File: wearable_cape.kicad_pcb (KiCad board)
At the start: 2 copper layers, 48 parts, among them P1 BELA_AINS, P2 RECEIVER, P3 BATTERY, P4 BELA_AOUTS, P5 CONN_01X04, P6 CONN_01X04, P7 CONN_01X04, SW1 SW_HALT, SW2 SW_MODE_SEL, U1 MCP6004, U2 MCP6004, U3 BEAGLEBONEBLACK, U4 OKI_7805

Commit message: basic routing done
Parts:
- added C20: 100nF, Capacitors_SMD:C_0603_HandSoldering, F.Cu at (87.6, 49.5)
- moved R1 34.7 mm to (88.3, 27.3)
- moved SW1 32.7 mm to (88.9, 31.8)
- moved R9 7.62 mm to (67.3, 58.4)
- moved R5 5.08 mm to (74.9, 58.4)
- moved R4 5.08 mm to (72.4, 58.4)
- moved R12 3.42 mm to (95.2, 68.6)
- moved R8 2.54 mm to (69.8, 58.4)
- moved SW2 1.27 mm to (102.2, 68.6)
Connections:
- C5 pad 2: GND -> GNDA
- P2 pad 2: /RCV0 -> /D15
- P2 pad 4: /RCV1 -> /D14
- P2 pad 6: /RCV2 -> /D13
- P2 pad 8: /RCV3 -> /D12
- P4 pad 10: Net-(P4-Pad10) -> GNDA
- P4 pad 9: Net-(P4-Pad9) -> VCC
- P5 pad 1: /FILT_OUT0 -> /FILT_OUT1
- P5 pad 2: /FILT_OUT1 -> /FILT_OUT0
- R2 pad 1: SYS_5V -> VCC
- R3 pad 2: GND -> GNDA
- R4 pad 2: /BELA_OUT0 -> /BELA_OUT2
- R5 pad 2: /BELA_OUT1 -> /BELA_OUT3
- R8 pad 2: /BELA_OUT2 -> /BELA_OUT1
- R9 pad 2: /BELA_OUT3 -> /BELA_OUT0
- U1 pad 11: GND -> GNDA
- U2 pad 11: GND -> GNDA
- U3 pad B10: /D2 -> /D3
- U3 pad B11: Net-(U3-PadB11) -> /D4
- U3 pad B12: /D4 -> /D5
- U3 pad B15: Net-(U3-PadB15) -> /D8
- U3 pad B16: /D8 -> /D9
- U3 pad B18: Net-(U3-PadB18) -> /D11
- U3 pad B2: Net-(U3-PadB2) -> GND
- U3 pad B27: /~HALT -> /D12
- U3 pad B28: /D12 -> /D13
- U3 pad B29: Net-(U3-PadB29) -> /D14
- U3 pad B3: SYS_3.3V -> Net-(U3-PadB3)
- U3 pad B30: /D14 -> /D15
- U3 pad B37: Net-(U3-PadB37) -> /TX
- U3 pad B38: Net-(U3-PadB38) -> /RX
- U3 pad B5: RAW_5V -> Net-(U3-PadB5)
- U3 pad B7: SYS_5V -> /D0
- U3 pad B8: /D0 -> /D1
- U3 pad B9: Net-(U3-PadB9) -> /D2
- U3 pad C10: /D3 -> Net-(U3-PadC10)
- U3 pad C11: /D6 -> Net-(U3-PadC11)
- U3 pad C12: /D5 -> /D6
- U3 pad C13: /D7 -> Net-(U3-PadC13)
- U3 pad C14: Net-(U3-PadC14) -> /D7
- U3 pad C15: /D10 -> Net-(U3-PadC15)
- U3 pad C16: /D9 -> /D10
- U3 pad C18: /D11 -> Net-(U3-PadC18)
- U3 pad C2: Net-(U3-PadC2) -> GND
- U3 pad C27: Net-(U3-PadC27) -> /~HALT
- U3 pad C28: /D13 -> Net-(U3-PadC28)
- U3 pad C30: /D15 -> Net-(U3-PadC30)
- U3 pad C4: Net-(U3-PadC4) -> SYS_3.3V
- U3 pad C43: Net-(U3-PadC43) -> GND
- U3 pad C44: Net-(U3-PadC44) -> GND
- U3 pad C45: Net-(U3-PadC45) -> GND
- U3 pad C46: Net-(U3-PadC46) -> GND
- U3 pad C6: Net-(U3-PadC6) -> RAW_5V
- U3 pad C7: Net-(U3-PadC7) -> SYS_5V
- U3 pad C8: /D1 -> Net-(U3-PadC8)
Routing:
- net GND: track 0.00 -> 135.3 mm, vias 0 -> 2
- net RAW_5V: track 0.00 -> 115.8 mm
- net BAT_11.1V: track 0.00 -> 110.1 mm
- net VCC: track 0.00 -> 63.7 mm, vias 0 -> 4
- net GNDA: track 0.00 -> 60.4 mm, vias 0 -> 2
- net /FILT_OUT5: track 0.00 -> 58.6 mm, vias 0 -> 2
- net SYS_3.3V: track 0.00 -> 54.1 mm
- net /FILT_OUT4: track 0.00 -> 53.1 mm, vias 0 -> 2
- net REF_1.8V: track 0.00 -> 52.9 mm, vias 0 -> 4
- net /FILT_OUT0: track 0.00 -> 45.2 mm, vias 0 -> 1
- net /FILT_OUT1: track 0.00 -> 43.2 mm, vias 0 -> 2
- net /~HALT: track 0.00 -> 34.3 mm
- net /FILT_OUT2: track 0.00 -> 32.1 mm
- net Net-(C10-Pad2): track 0.00 -> 31.4 mm, vias 0 -> 2
- net /D15: track 0.00 -> 31.4 mm
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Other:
- net class BAT added: clearance 0.3, trace_width 0.5, via_dia 1, via_drill 0.6

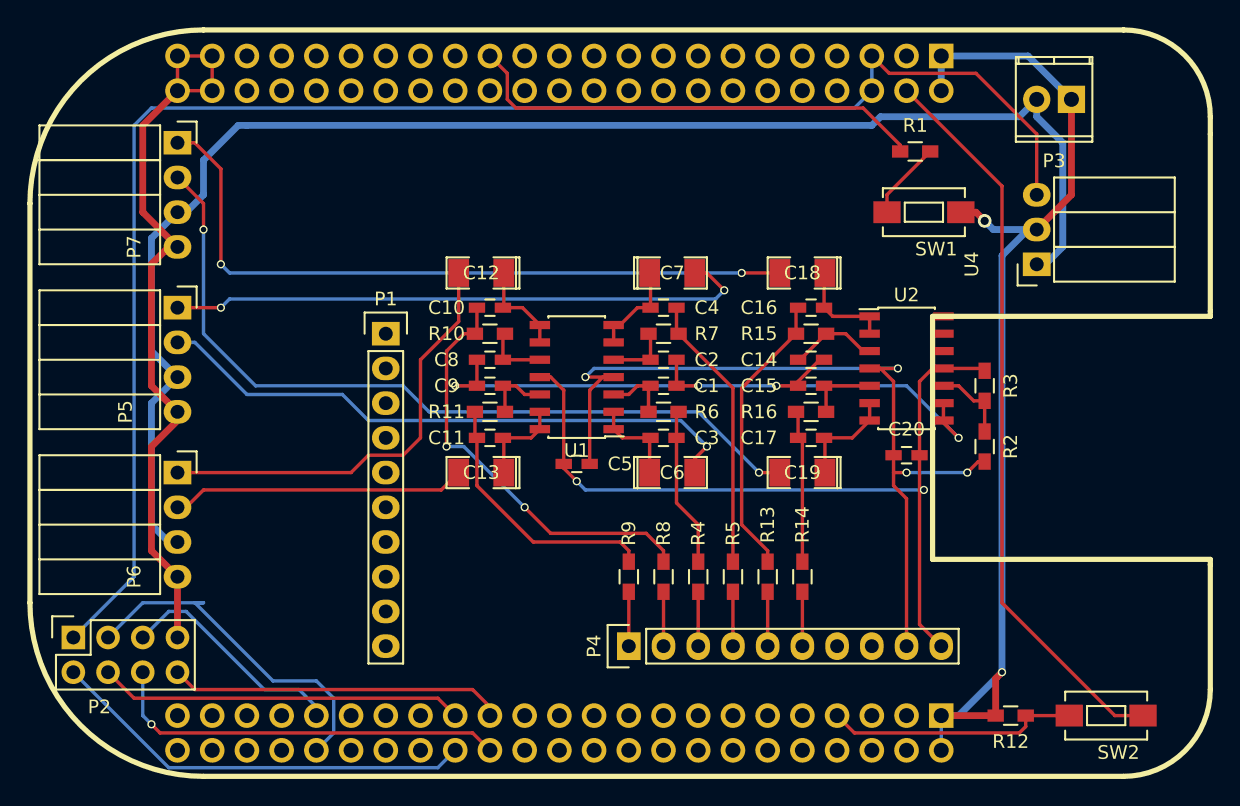
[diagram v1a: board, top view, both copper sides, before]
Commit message: added zones
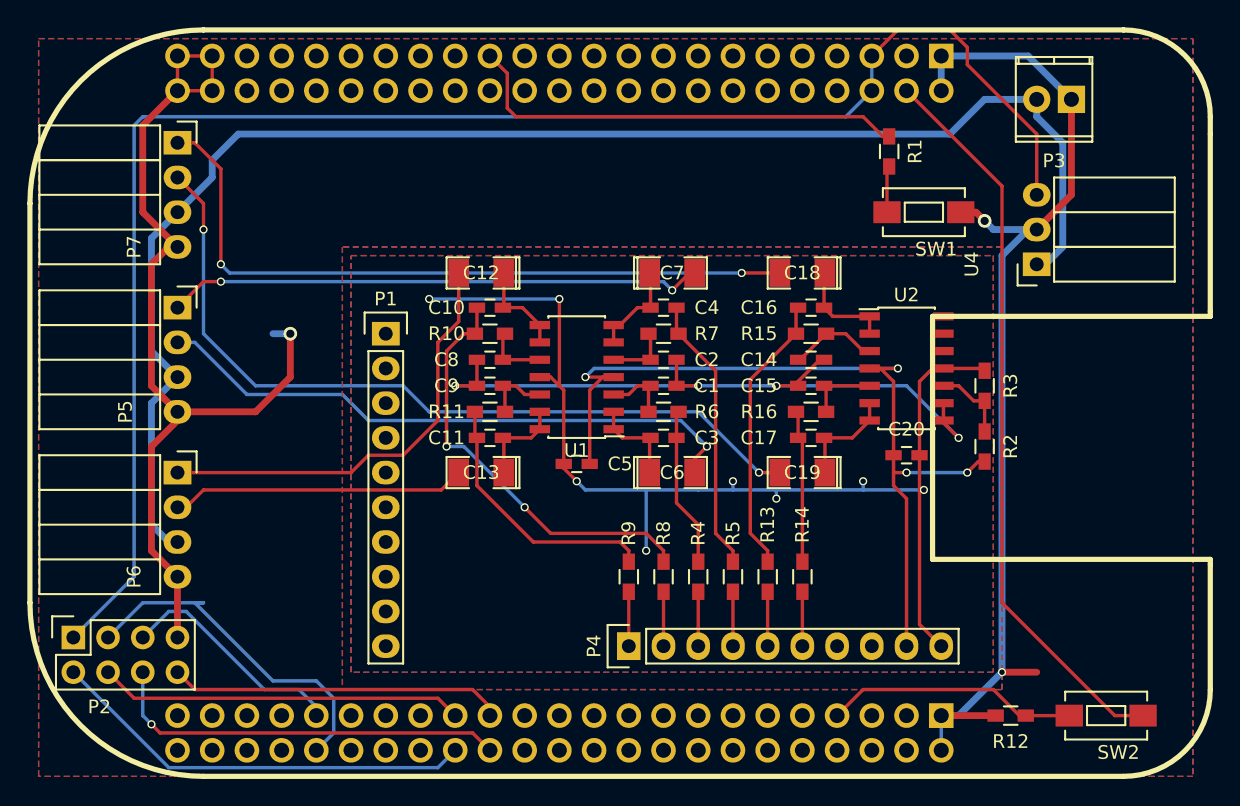
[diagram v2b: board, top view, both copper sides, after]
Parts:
- moved R1 1.91 mm to (86.4, 27.3), turned to 270 degrees
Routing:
- net GNDA: track 60.4 -> 82.7 mm, vias 2 -> 8
- net GND: track 135.3 -> 148.2 mm, vias 2 -> 3
- net /FILT_OUT1: track 43.2 -> 39.4 mm
- net Net-(R1-Pad2): track 5.76 -> 3.41 mm
- net RAW_5V: track 115.8 -> 118.1 mm
- net /~HALT: track 34.3 -> 33.1 mm
- net Net-(C16-Pad2): track 21.1 -> 20.6 mm
- added copper zone on B.Cu, net GND
- added copper zone on F.Cu, net GND
- added copper zone on B.Cu, net GNDA
- added copper zone on F.Cu, net GNDA

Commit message: Updates to PCB and first BOM files
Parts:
- added C21: CP1, SMD_Packages:SMD-1210_Pol, F.Cu at (91.2, 34.8)
- added C22: CP1, SMD_Packages:SMD-1210_Pol, F.Cu at (93.0, 29.2)
- moved SW2 7.75 mm to (97.8, 62.2), turned to 270 degrees
- moved P2 7.62 mm to (34.3, 62.9)
- moved P5 7.62 mm to (41.9, 38.7)
- moved P6 7.62 mm to (41.9, 50.8)
- moved P7 7.62 mm to (41.9, 26.7)
- moved R1 5.64 mm to (80.9, 28.7)
- moved SW1 3.78 mm to (86.4, 29.0)
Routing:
- net GND: track 148.2 -> 195.3 mm, vias 3 -> 1
- net SYS_3.3V: track 54.1 -> 42.4 mm
- net /FILT_OUT4: track 53.1 -> 41.5 mm, vias 2 -> 0
- net /FILT_OUT0: track 45.2 -> 35.6 mm
- net /FILT_OUT2: track 32.1 -> 23.1 mm
- net /FILT_OUT3: track 21.6 -> 14.0 mm
- net /D14: track 26.7 -> 19.1 mm
- net /D13: track 29.6 -> 22.0 mm, vias 1 -> 0
- net /D12: track 24.5 -> 17.7 mm
- net /D15: track 31.4 -> 24.5 mm
- net /FILT_OUT1: track 39.4 -> 33.8 mm, vias 2 -> 0
- net /RX: track 26.1 -> 20.5 mm
- net BAT_11.1V: track 110.0 -> 105.5 mm
- net /FILT_OUT5: track 58.6 -> 54.2 mm
- net /~HALT: track 33.1 -> 28.8 mm
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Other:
- board outline added: 70.5 x 54.6 mm

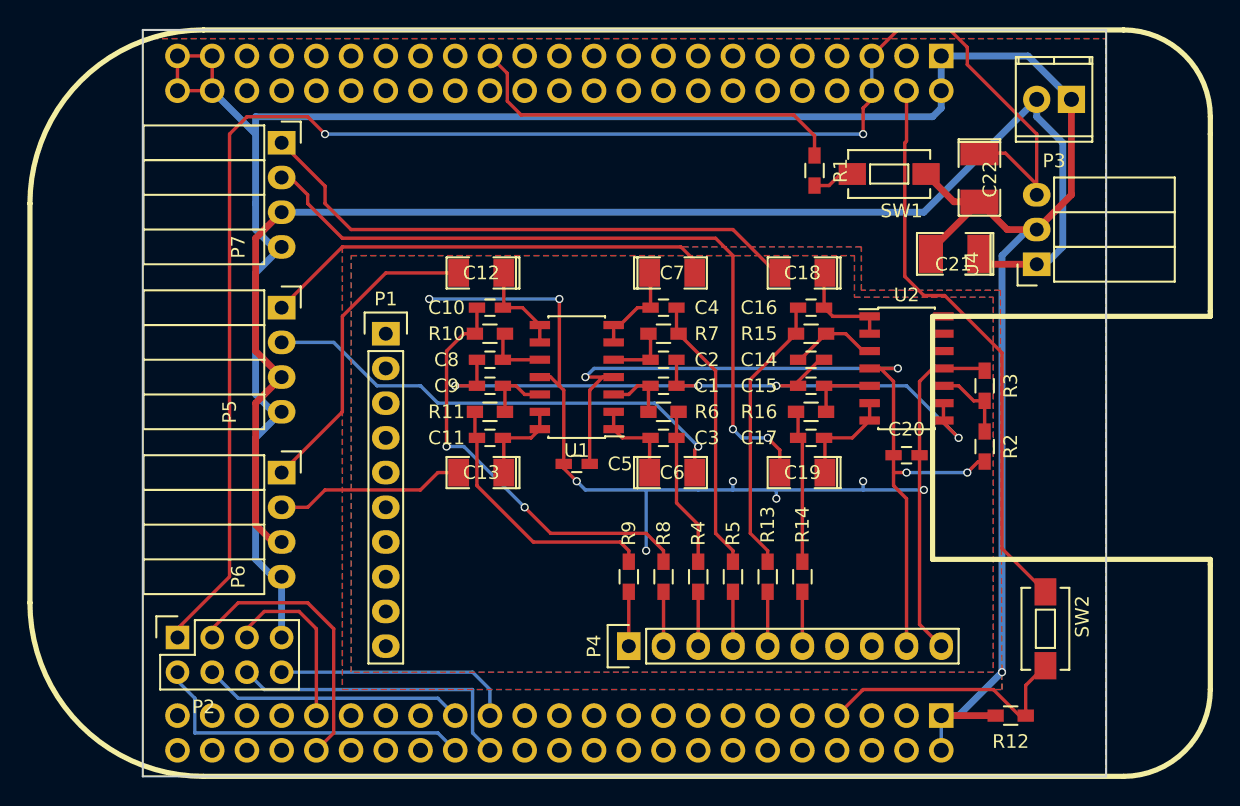
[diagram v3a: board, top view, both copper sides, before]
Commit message: Fill in zones better
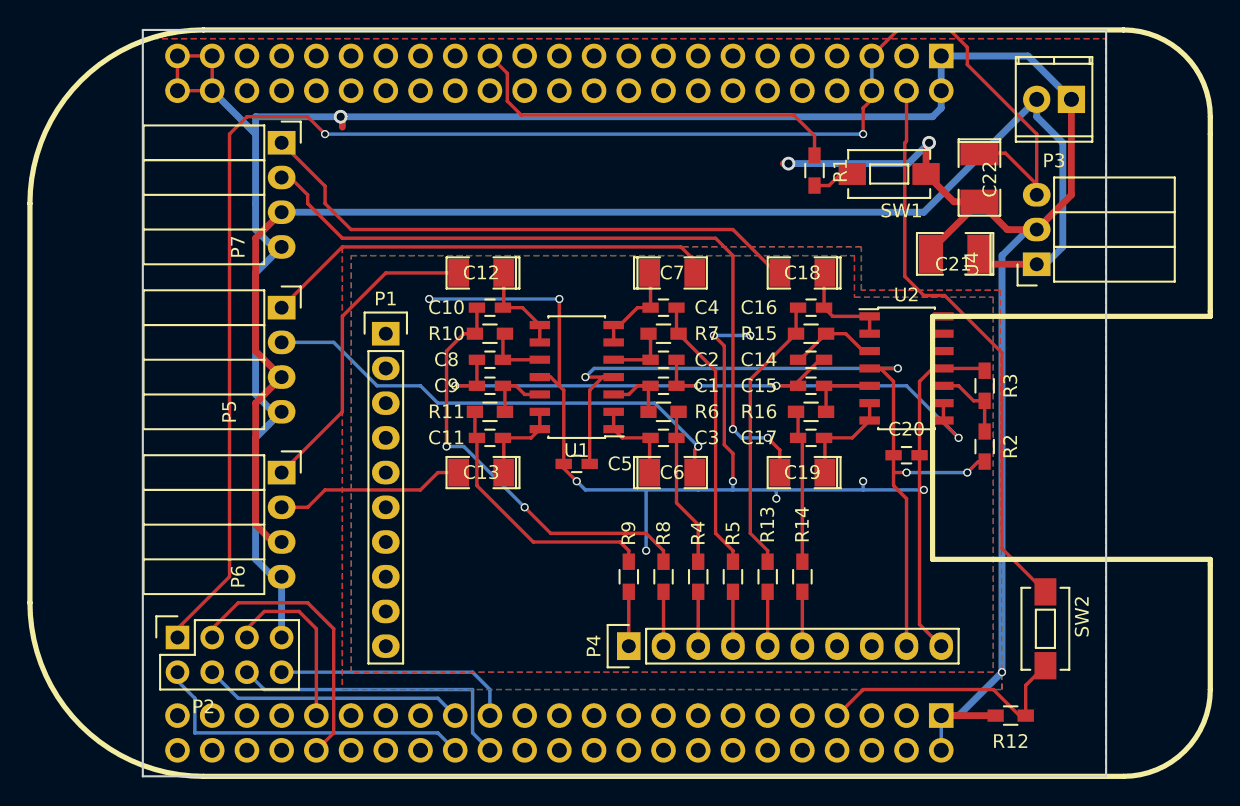
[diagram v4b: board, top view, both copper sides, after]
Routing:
- net GND: track 195.3 -> 209.7 mm, vias 1 -> 4
- net GNDA: track 82.7 -> 96.6 mm, vias 8 -> 10
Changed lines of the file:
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@@
     (links 110)
     (no_connects 0)
-    (area 31.674999 18.339999 102.310001 73.100001)
+    (area 23.004499 17.76912 110.345501 73.515501)
     (thickness 1.6)
     (drawings 4)
-    (tracks 358)
+    (tracks 376)
     (zones 0)
     (modules 51)
@@
     (visible_elements FFFFFF7F)
     (pcbplotparams
-      (layerselection 0x00030_80000001)
+      (layerselection 0x010fc_80000001)
       (usegerberextensions false)
-      (excludeedgelayer true)
+      (excludeedgelayer false)
       (linewidth 0.100000)
       (plotframeref false)
       (viasonmask false)
       (mode 1)
-      (useauxorigin false)
+      (useauxorigin true)
       (hpglpennumber 1)
       (hpglpenspeed 20)
@@
       (plotinvisibletext false)
       (padsonsilk false)
-      (subtractmaskfromsilk false)
+      (subtractmaskfromsilk true)
       (outputformat 1)
       (mirror false)
-      (drillshape 1)
+      (drillshape 0)
       (scaleselection 1)
-      (outputdirectory ""))
+      (outputdirectory gerber/))
   )
   (net 0 "")
@@
   (segment (start 65.405 43.815) (end 66.2 43.815) (width 0.25) (layer F.Cu) (net 8))
   (segment (start 64.45 44.77) (end 65.405 43.815) (width 0.25) (layer F.Cu) (net 8))
+  (via (at 46.228 24.765) (size 1) (drill 0.6) (layers F.Cu B.Cu) (net 9))
+  (segment (start 46.355 25.527) (end 46.355 24.892) (width 0.5) (layer F.Cu) (net 9))
+  (segment (start 46.355 24.892) (end 46.228 24.765) (width 0.5) (layer F.Cu) (net 9))
+  (segment (start 89.06 28.956) (end 89.06 26.891) (width 0.5) (layer F.Cu) (net 9))
+  (segment (start 78.994 28.194) (end 78.613 28.194) (width 0.5) (layer F.Cu) (net 9))
+  (via (at 78.994 28.194) (size 1) (drill 0.6) (layers F.Cu B.Cu) (net 9))
+  (segment (start 87.757 28.194) (end 78.994 28.194) (width 0.5) (layer B.Cu) (net 9))
+  (segment (start 89.281 26.67) (end 87.757 28.194) (width 0.5) (layer B.Cu) (net 9))
+  (via (at 89.281 26.67) (size 1) (drill 0.6) (layers F.Cu B.Cu) (net 9))
+  (segment (start 89.06 26.891) (end 89.281 26.67) (width 0.5) (layer F.Cu) (net 9))
   (segment (start 92.964 30.988) (end 91.092 30.988) (width 0.5) (layer F.Cu) (net 9))
   (segment (start 91.092 30.988) (end 89.06 28.956) (width 0.5) (layer F.Cu) (net 9))
@@
   (segment (start 90.17 22.86) (end 90.17 24.13) (width 0.5) (layer B.Cu) (net 9))
   (segment (start 40.005 24.765) (end 40.005 26.035) (width 0.5) (layer B.Cu) (net 9))
-  (segment (start 89.535 24.765) (end 40.005 24.765) (width 0.5) (layer B.Cu) (net 9))
+  (segment (start 89.535 24.765) (end 46.228 24.765) (width 0.5) (layer B.Cu) (net 9))
+  (segment (start 46.228 24.765) (end 40.005 24.765) (width 0.5) (layer B.Cu) (net 9))
   (segment (start 90.17 24.13) (end 89.535 24.765) (width 0.5) (layer B.Cu) (net 9))
   (segment (start 41.91 62.865) (end 41.91 58.42) (width 0.5) (layer B.Cu) (net 9))
@@
   (segment (start 43.18 60.96) (end 44.45 62.23) (width 0.25) (layer F.Cu) (net 121))
   (segment (start 44.45 62.23) (end 44.45 68.58) (width 0.25) (layer F.Cu) (net 121))
+  (segment (start 74.93 51.435) (end 74.93 49.403) (width 0.25) (layer F.Cu) (net 122))
+  (via (at 74.93 51.435) (size 0.6) (drill 0.4) (layers F.Cu B.Cu) (net 122))
+  (segment (start 74.93 52.07) (end 74.93 51.435) (width 0.25) (layer B.Cu) (net 122))
+  (via (at 76.2 40.767) (size 0.6) (drill 0.4) (layers F.Cu B.Cu) (net 122))
+  (segment (start 73.533 40.767) (end 76.2 40.767) (width 0.25) (layer B.Cu) (net 122))
+  (via (at 73.533 40.767) (size 0.6) (drill 0.4) (layers F.Cu B.Cu) (net 122))
+  (segment (start 74.295 41.529) (end 73.533 40.767) (width 0.25) (layer F.Cu) (net 122))
+  (segment (start 74.295 48.768) (end 74.295 41.529) (width 0.25) (layer F.Cu) (net 122))
+  (segment (start 74.93 49.403) (end 74.295 48.768) (width 0.25) (layer F.Cu) (net 122))
   (segment (start 62.23 44.45) (end 62.23 38.1) (width 0.25) (layer F.Cu) (net 122))
   (via (at 52.705 38.1) (size 0.6) (drill 0.4) (layers F.Cu B.Cu) (net 122))
@@
   (segment (start 84.455 52.07) (end 84.455 51.435) (width 0.25) (layer B.Cu) (net 122))
   (via (at 84.455 51.435) (size 0.6) (drill 0.4) (layers F.Cu B.Cu) (net 122))
-  (segment (start 74.93 52.07) (end 74.93 51.435) (width 0.25) (layer B.Cu) (net 122))
-  (via (at 74.93 51.435) (size 0.6) (drill 0.4) (layers F.Cu B.Cu) (net 122))
   (segment (start 62.55 50.165) (end 62.55 50.485) (width 0.25) (layer F.Cu) (net 122))
   (segment (start 62.55 50.485) (end 63.5 51.435) (width 0.25) (layer F.Cu) (net 122))
